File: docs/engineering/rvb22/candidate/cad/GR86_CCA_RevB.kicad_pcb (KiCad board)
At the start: 4 copper layers, 88.3 x 61.3 mm, 199 parts, among them J201 TC2030-IDC-NL / UART, J202 RESET — short to reset, J203 BOOT — hold low on reset, J401 U.FL-R-SMT-1(80), Q101 STD25NF20 /200V, U101 LTC4367HMS8#WTRPBF, U121 LM5164DDAR, U151 LM63615DQPWPRQ1, U201 ESP32-S3-WROOM-1-N8R2, U202 TPS3808G33-Q1 3.07V RESET, U301 TCAN3403DRBRQ1, U401 PA1616D, U402 SN74LVC2G125DCUR, U403 MIC5504-3.3YM5-TR, U404 SN74LVC2G125DCUR, U501 TPS26600PWPR, U502 OPA2333AIDR

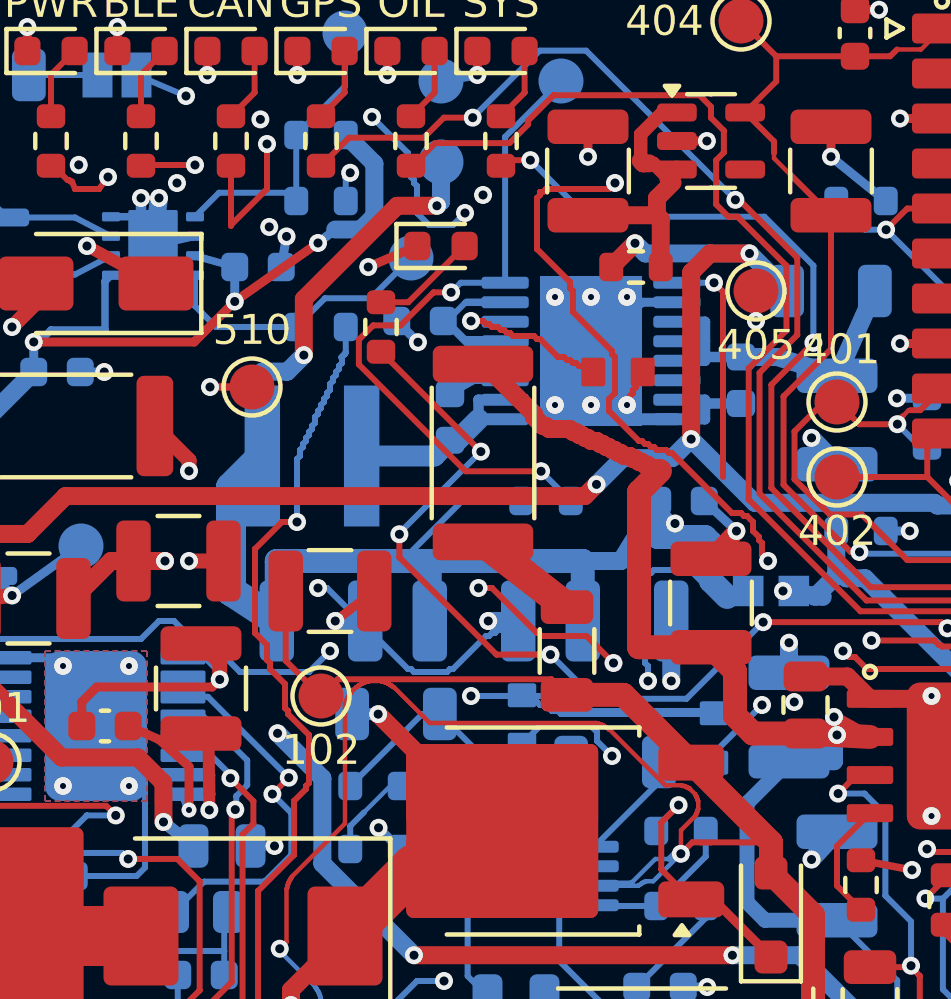
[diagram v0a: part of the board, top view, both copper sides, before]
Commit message: fix(cca): apply I08 native routing and source integrity corrections
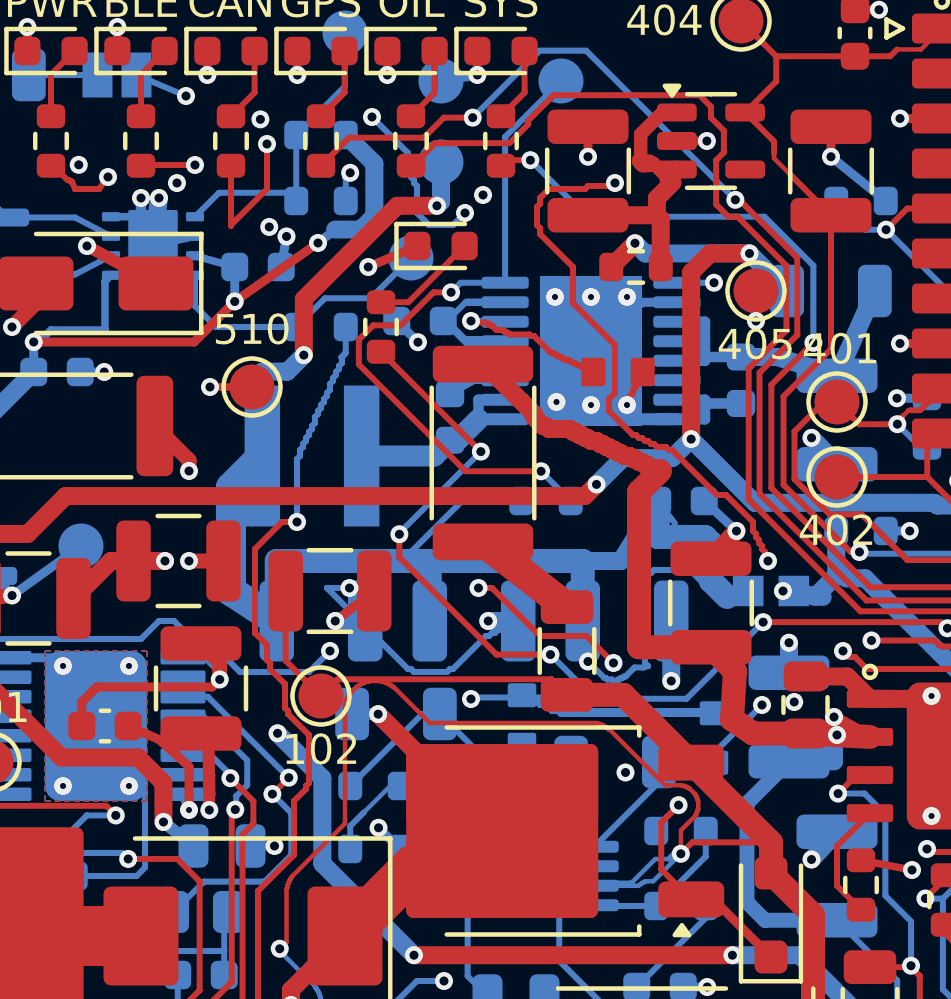
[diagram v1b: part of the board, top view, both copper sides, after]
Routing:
- net GND: track 197.0 -> 179.3 mm
- net 3V3_FB_ADJ: track 70.7 -> 64.0 mm
- net +3V3: track 331.9 -> 338.3 mm
- net 3V3_SOURCE: track 68.7 -> 72.9 mm, vias 5 -> 4
- net 3V3_VCC_INTERNAL: track 11.6 -> 10.3 mm

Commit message: fix(cca): route rail around mechanical holes and resolve native model exports
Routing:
- net +3V3: track 338.3 -> 350.1 mm
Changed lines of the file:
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@@
 (segment (start 40.7 19.6) (end 40.8 19.7) (width 0.2) (layer "F.Cu") (net 132))
 (segment (start 40.8 19.7) (end 40.9 20.0) (width 0.2) (layer "F.Cu") (net 132))
-(segment (start 57.9 16.8) (end 58.0 16.5) (width 2.0) (layer "In2.Cu") (net 1))
-(segment (start 58.0 16.5) (end 63.7 10.8) (width 2.0) (layer "In2.Cu") (net 1))
-(segment (start 63.7 10.8) (end 63.7 7.7) (width 2.0) (layer "In2.Cu") (net 1))
-(segment (start 63.7 7.7) (end 63.8 7.6) (width 2.0) (layer "In2.Cu") (net 1))
-(segment (start 63.8 7.6) (end 63.8 7.4) (width 2.0) (layer "In2.Cu") (net 1))
-(segment (start 63.8 7.4) (end 64.3 6.9) (width 2.0) (layer "In2.Cu") (net 1))
-(segment (start 64.3 6.9) (end 64.3 6.1) (width 2.0) (layer "In2.Cu") (net 1))
-(segment (start 64.3 6.1) (end 64.4 6.0) (width 2.0) (layer "In2.Cu") (net 1))
-(segment (start 64.4 6.0) (end 64.4 5.9) (width 2.0) (layer "In2.Cu") (net 1))
-(segment (start 64.4 5.9) (end 64.5 5.8) (width 2.0) (layer "In2.Cu") (net 1))
-(segment (start 64.5 5.8) (end 64.5 5.7) (width 2.0) (layer "In2.Cu") (net 1))
-(segment (start 64.5 5.7) (end 65.0 5.2) (width 2.0) (layer "In2.Cu") (net 1))
-(segment (start 65.0 5.2) (end 65.1 5.2) (width 2.0) (layer "In2.Cu") (net 1))
-(segment (start 65.1 5.2) (end 65.2 5.1) (width 2.0) (layer "In2.Cu") (net 1))
-(segment (start 65.2 5.1) (end 65.5 5.1) (width 2.0) (layer "In2.Cu") (net 1))
-(segment (start 65.5 5.1) (end 65.6 5.0) (width 2.0) (layer "In2.Cu") (net 1))
-(segment (start 65.6 5.0) (end 66.4 5.0) (width 2.0) (layer "In2.Cu") (net 1))
-(segment (start 66.4 5.0) (end 70.6 9.2) (width 2.0) (layer "In2.Cu") (net 1))
-(segment (start 70.6 9.2) (end 70.7 9.2) (width 2.0) (layer "In2.Cu") (net 1))
-(segment (start 70.7 9.2) (end 70.8 9.3) (width 2.0) (layer "In2.Cu") (net 1))
-(segment (start 70.8 9.3) (end 70.9 9.3) (width 2.0) (layer "In2.Cu") (net 1))
-(segment (start 70.9 9.3) (end 71.0 9.4) (width 2.0) (layer "In2.Cu") (net 1))
-(segment (start 71.0 9.4) (end 71.1 9.4) (width 2.0) (layer "In2.Cu") (net 1))
-(segment (start 71.1 9.4) (end 71.2 9.5) (width 2.0) (layer "In2.Cu") (net 1))
-(segment (start 71.2 9.5) (end 71.5 9.6) (width 2.0) (layer "In2.Cu") (net 1))
 (segment (start 34.9 23.35) (end 35.6 24.05) (width 0.2) (layer "In2.Cu") (net 5))
 (segment (start 35.6 24.05) (end 36.55 24.05) (width 0.2) (layer "In2.Cu") (net 5))
@@
 (segment (start 34.9 13.6) (end 34.95 13.65) (width 0.2) (layer "F.Cu") (net 131))
 (segment (start 34.95 13.65) (end 35.075 13.7) (width 0.2) (layer "F.Cu") (net 131))
+(segment (start 57.9 16.8) (end 58.0 16.5) (width 2.0) (layer "In2.Cu") (net 1))
+(segment (start 58.0 16.5) (end 63.7 10.8) (width 2.0) (layer "In2.Cu") (net 1))
+(segment (start 63.7 10.8) (end 63.7 7.7) (width 2.0) (layer "In2.Cu") (net 1))
+(segment (start 63.7 7.7) (end 63.8 7.6) (width 2.0) (layer "In2.Cu") (net 1))
+(segment (start 63.8 7.6) (end 63.8 7.4) (width 2.0) (layer "In2.Cu") (net 1))
+(segment (start 63.8 7.4) (end 64.3 6.9) (width 2.0) (layer "In2.Cu") (net 1))
+(segment (start 64.3 6.9) (end 64.3 6.1) (width 2.0) (layer "In2.Cu") (net 1))
+(segment (start 64.3 6.1) (end 64.4 6.0) (width 2.0) (layer "In2.Cu") (net 1))
+(segment (start 64.4 6.0) (end 64.4 5.9) (width 2.0) (layer "In2.Cu") (net 1))
+(segment (start 64.4 5.9) (end 64.5 5.8) (width 2.0) (layer "In2.Cu") (net 1))
+(segment (start 64.5 5.8) (end 64.5 5.7) (width 2.0) (layer "In2.Cu") (net 1))
+(segment (start 64.5 5.7) (end 65.0 5.2) (width 2.0) (layer "In2.Cu") (net 1))
+(segment (start 65.0 5.2) (end 65.1 5.2) (width 2.0) (layer "In2.Cu") (net 1))
+(segment (start 65.1 5.2) (end 65.2 5.1) (width 2.0) (layer "In2.Cu") (net 1))
+(segment (start 65.2 5.1) (end 65.5 5.1) (width 2.0) (layer "In2.Cu") (net 1))
+(segment (start 65.5 5.1) (end 65.6 5.0) (width 2.0) (layer "In2.Cu") (net 1))
+(segment (start 65.6 5.0) (end 66.7 5.0) (width 2.0) (layer "In2.Cu") (net 1))
+(segment (start 66.7 5.0) (end 68.1 3.6) (width 2.0) (layer "In2.Cu") (net 1))
+(segment (start 68.1 3.6) (end 68.2 3.6) (width 2.0) (layer "In2.Cu") (net 1))
+(segment (start 68.2 3.6) (end 68.4 3.4) (width 2.0) (layer "In2.Cu") (net 1))
+(segment (start 68.4 3.4) (end 68.5 3.4) (width 2.0) (layer "In2.Cu") (net 1))
+(segment (start 68.5 3.4) (end 68.6 3.3) (width 2.0) (layer "In2.Cu") (net 1))
+(segment (start 68.6 3.3) (end 68.9 3.3) (width 2.0) (layer "In2.Cu") (net 1))
+(segment (start 68.9 3.3) (end 69.0 3.2) (width 2.0) (layer "In2.Cu") (net 1))
+(segment (start 69.0 3.2) (end 73.9 3.2) (width 2.0) (layer "In2.Cu") (net 1))
+(segment (start 73.9 3.2) (end 74.0 3.3) (width 2.0) (layer "In2.Cu") (net 1))
+(segment (start 74.0 3.3) (end 74.2 3.3) (width 2.0) (layer "In2.Cu") (net 1))
+(segment (start 74.2 3.3) (end 74.3 3.4) (width 2.0) (layer "In2.Cu") (net 1))
+(segment (start 74.3 3.4) (end 74.4 3.4) (width 2.0) (layer "In2.Cu") (net 1))
+(segment (start 74.4 3.4) (end 74.5 3.5) (width 2.0) (layer "In2.Cu") (net 1))
+(segment (start 74.5 3.5) (end 74.6 3.5) (width 2.0) (layer "In2.Cu") (net 1))
+(segment (start 74.6 3.5) (end 75.0 3.9) (width 2.0) (layer "In2.Cu") (net 1))
+(segment (start 75.0 3.9) (end 75.0 4.0) (width 2.0) (layer "In2.Cu") (net 1))
+(segment (start 75.0 4.0) (end 75.1 4.1) (width 2.0) (layer "In2.Cu") (net 1))
+(segment (start 75.1 4.1) (end 75.1 4.2) (width 2.0) (layer "In2.Cu") (net 1))
+(segment (start 75.1 4.2) (end 75.2 4.3) (width 2.0) (layer "In2.Cu") (net 1))
+(segment (start 75.2 4.3) (end 75.2 4.4) (width 2.0) (layer "In2.Cu") (net 1))
+(segment (start 75.2 4.4) (end 75.3 4.5) (width 2.0) (layer "In2.Cu") (net 1))
+(segment (start 75.3 4.5) (end 75.3 4.6) (width 2.0) (layer "In2.Cu") (net 1))
+(segment (start 75.3 4.6) (end 75.8 5.1) (width 2.0) (layer "In2.Cu") (net 1))
+(segment (start 75.8 5.1) (end 75.8 5.2) (width 2.0) (layer "In2.Cu") (net 1))
+(segment (start 75.8 5.2) (end 76.0 5.4) (width 2.0) (layer "In2.Cu") (net 1))
+(segment (start 76.0 5.4) (end 76.0 5.6) (width 2.0) (layer "In2.Cu") (net 1))
+(segment (start 76.0 5.6) (end 76.1 5.7) (width 2.0) (layer "In2.Cu") (net 1))
+(segment (start 76.1 5.7) (end 76.1 6.3) (width 2.0) (layer "In2.Cu") (net 1))
+(segment (start 76.1 6.3) (end 76.0 6.4) (width 2.0) (layer "In2.Cu") (net 1))
+(segment (start 76.0 6.4) (end 76.0 6.6) (width 2.0) (layer "In2.Cu") (net 1))
+(segment (start 76.0 6.6) (end 75.8 6.8) (width 2.0) (layer "In2.Cu") (net 1))
+(segment (start 75.8 6.8) (end 75.8 6.9) (width 2.0) (layer "In2.Cu") (net 1))
+(segment (start 75.8 6.9) (end 75.3 7.4) (width 2.0) (layer "In2.Cu") (net 1))
+(segment (start 75.3 7.4) (end 75.3 7.5) (width 2.0) (layer "In2.Cu") (net 1))
+(segment (start 75.3 7.5) (end 75.2 7.6) (width 2.0) (layer "In2.Cu") (net 1))
+(segment (start 75.2 7.6) (end 75.2 7.7) (width 2.0) (layer "In2.Cu") (net 1))
+(segment (start 75.2 7.7) (end 75.1 7.8) (width 2.0) (layer "In2.Cu") (net 1))
+(segment (start 75.1 7.8) (end 75.1 7.9) (width 2.0) (layer "In2.Cu") (net 1))
+(segment (start 75.1 7.9) (end 75.0 8.0) (width 2.0) (layer "In2.Cu") (net 1))
+(segment (start 75.0 8.0) (end 75.0 8.1) (width 2.0) (layer "In2.Cu") (net 1))
+(segment (start 75.0 8.1) (end 74.6 8.5) (width 2.0) (layer "In2.Cu") (net 1))
+(segment (start 74.6 8.5) (end 74.5 8.5) (width 2.0) (layer "In2.Cu") (net 1))
+(segment (start 74.5 8.5) (end 74.4 8.6) (width 2.0) (layer "In2.Cu") (net 1))
+(segment (start 74.4 8.6) (end 74.3 8.6) (width 2.0) (layer "In2.Cu") (net 1))
+(segment (start 74.3 8.6) (end 74.2 8.7) (width 2.0) (layer "In2.Cu") (net 1))
+(segment (start 74.2 8.7) (end 74.0 8.7) (width 2.0) (layer "In2.Cu") (net 1))
+(segment (start 74.0 8.7) (end 73.9 8.8) (width 2.0) (layer "In2.Cu") (net 1))
+(segment (start 73.9 8.8) (end 73.2 8.8) (width 2.0) (layer "In2.Cu") (net 1))
+(segment (start 73.2 8.8) (end 73.1 8.9) (width 2.0) (layer "In2.Cu") (net 1))
+(segment (start 73.1 8.9) (end 73.0 8.9) (width 2.0) (layer "In2.Cu") (net 1))
+(segment (start 73.0 8.9) (end 72.9 9.0) (width 2.0) (layer "In2.Cu") (net 1))
+(segment (start 72.9 9.0) (end 72.8 9.0) (width 2.0) (layer "In2.Cu") (net 1))
+(segment (start 72.8 9.0) (end 72.7 9.1) (width 2.0) (layer "In2.Cu") (net 1))
+(segment (start 72.7 9.1) (end 72.3 9.1) (width 2.0) (layer "In2.Cu") (net 1))
+(segment (start 72.3 9.1) (end 72.2 9.2) (width 2.0) (layer "In2.Cu") (net 1))
+(segment (start 72.2 9.2) (end 72.0 9.2) (width 2.0) (layer "In2.Cu") (net 1))
+(segment (start 72.0 9.2) (end 71.9 9.3) (width 2.0) (layer "In2.Cu") (net 1))
+(segment (start 71.9 9.3) (end 71.8 9.3) (width 2.0) (layer "In2.Cu") (net 1))
+(segment (start 71.8 9.3) (end 71.5 9.6) (width 2.0) (layer "In2.Cu") (net 1))
 )

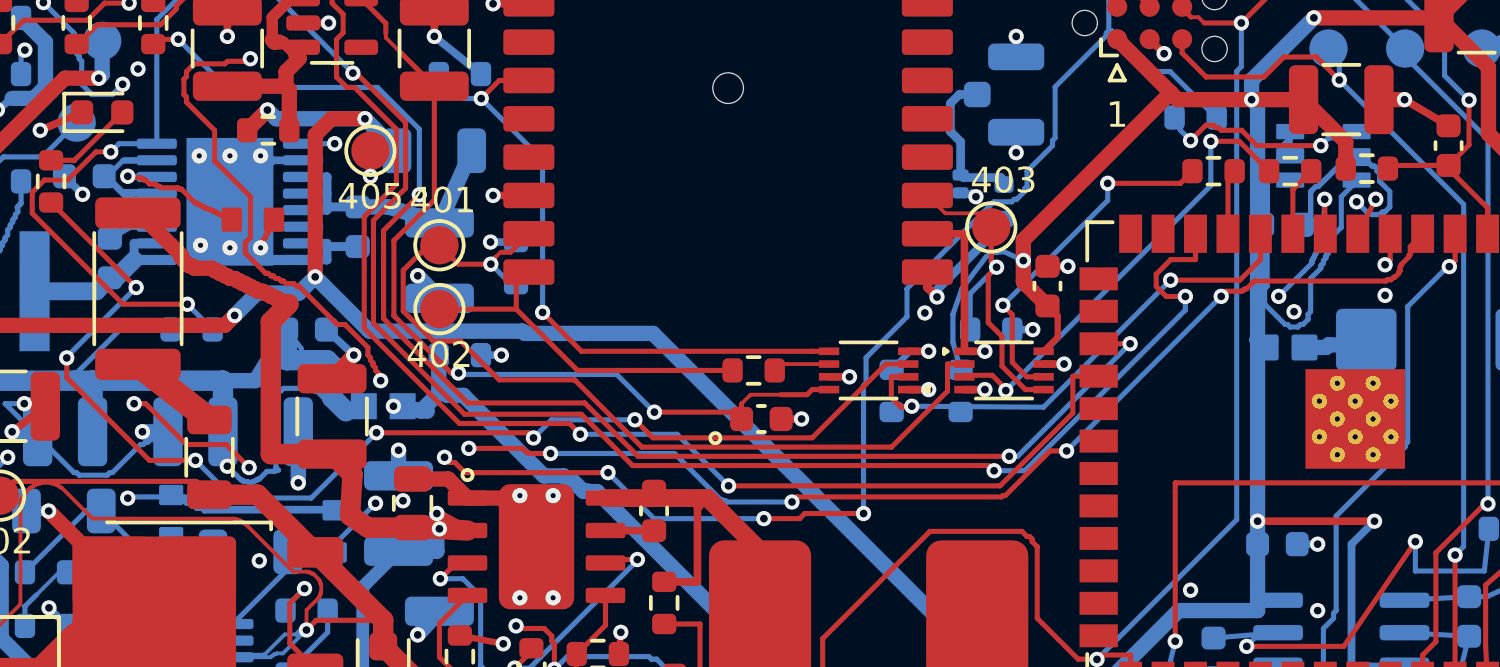
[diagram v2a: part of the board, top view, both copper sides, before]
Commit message: fix(cca): remove duplicate rail branch and select explicit native footprint exporter
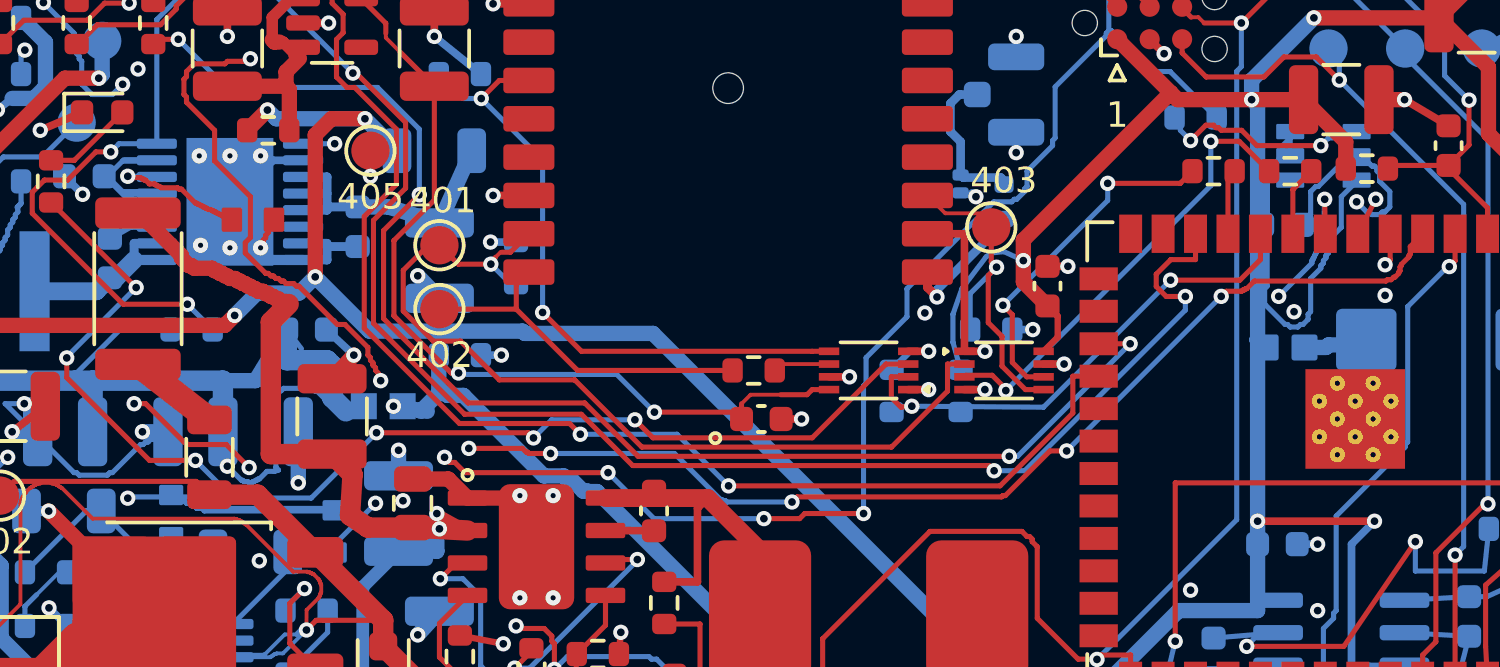
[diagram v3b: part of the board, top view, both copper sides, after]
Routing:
- net +3V3: track 350.1 -> 347.2 mm
- net GND: track 179.3 -> 176.6 mm
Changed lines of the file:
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@@
 (segment (start 77.0 13.8) (end 77.0 13.9) (width 0.2) (layer "B.Cu") (net 30))
 (segment (start 77.0 13.9) (end 76.97500000000001 13.9) (width 0.2) (layer "B.Cu") (net 30))
-(segment (start 76.97500000000001 13.9) (end 77.0 13.9) (width 0.2) (layer "B.Cu") (net 30))
 (segment (start 77.0 13.9) (end 77.1 13.8) (width 0.2) (layer "B.Cu") (net 30))
 (segment (start 77.1 13.8) (end 77.1 13.7) (width 0.2) (layer "B.Cu") (net 30))
 (segment (start 77.1 13.7) (end 77.3 13.5) (width 0.2) (layer "B.Cu") (net 30))
-(segment (start 77.3 13.5) (end 77.3 12.6) (width 0.2) (layer "B.Cu") (net 30))
-(segment (start 77.3 12.6) (end 77.5 12.4) (width 0.2) (layer "B.Cu") (net 30))
-(segment (start 77.5 12.4) (end 77.6 12.4) (width 0.2) (layer "B.Cu") (net 30))
-(segment (start 77.6 12.4) (end 78.4 11.6) (width 0.2) (layer "B.Cu") (net 30))
-(segment (start 78.4 11.6) (end 78.5 11.6) (width 0.2) (layer "B.Cu") (net 30))
-(segment (start 78.5 11.6) (end 78.6 11.5) (width 0.2) (layer "B.Cu") (net 30))
 (segment (start 78.6 11.5) (end 79.6 11.5) (width 0.2) (layer "B.Cu") (net 30))
 (segment (start 79.6 11.5) (end 79.7 11.6) (width 0.2) (layer "B.Cu") (net 30))
@@
 (segment (start 76.5 10.25) (end 76.5 11.2) (width 0.2) (layer "B.Cu") (net 1))
 (segment (start 76.5 11.2) (end 76.2 11.2) (width 0.2) (layer "B.Cu") (net 1))
-(segment (start 76.2 11.2) (end 75.7 11.7) (width 0.2) (layer "B.Cu") (net 1))
-(segment (start 75.7 11.7) (end 75.7 11.8) (width 0.2) (layer "B.Cu") (net 1))
-(segment (start 75.7 11.8) (end 75.6 11.9) (width 0.2) (layer "B.Cu") (net 1))
 (segment (start 75.6 11.9) (end 75.6 16.3) (width 0.2) (layer "B.Cu") (net 1))
 (segment (start 75.6 16.3) (end 75.5 16.4) (width 0.2) (layer "B.Cu") (net 1))
@@
 (segment (start 79.0 12.2) (end 79.1 12.1) (width 0.2) (layer "B.Cu") (net 1))
 (segment (start 79.1 12.1) (end 79.1 12.149999999999999) (width 0.2) (layer "B.Cu") (net 1))
-(segment (start 75.425 13.9) (end 75.4 13.9) (width 0.2) (layer "B.Cu") (net 1))
 (segment (start 75.4 13.9) (end 75.4 9.8) (width 0.2) (layer "B.Cu") (net 1))
 (segment (start 75.4 9.8) (end 75.3 9.7) (width 0.2) (layer "B.Cu") (net 1))
@@
 (segment (start 86.5 14.8) (end 86.6 14.7) (width 0.6) (layer "F.Cu") (net 30))
 (segment (start 85.8 16.3) (end 85.9 16.2) (width 0.6) (layer "F.Cu") (net 30))
-(segment (start 71.5 9.6) (end 71.8 9.3) (width 2.0) (layer "In2.Cu") (net 1))
 (segment (start 34.5 24.5) (end 35.0 25.0) (width 0.2) (layer "B.Cu") (net 132))
 (segment (start 36.6 14.0) (end 36.5 14.1) (width 0.2) (layer "F.Cu") (net 30))
@@
 (segment (start 30.4 11.8) (end 30.8 11.4) (width 0.2) (layer "B.Cu") (net 7))
 (segment (start 63.55 8.8) (end 64.25 8.8) (width 0.34) (layer "B.Cu") (net 34))
-(segment (start 71.9 9.3) (end 72.0 9.2) (width 2.0) (layer "In2.Cu") (net 1))
 (segment (start 37.5 24.6) (end 37.4 24.5) (width 0.2) (layer "In2.Cu") (net 5))
 (segment (start 40.5 24.6) (end 37.5 24.6) (width 0.2) (layer "In2.Cu") (net 5))
@@
 (segment (start 50.3 20.1) (end 50.6 20.1) (width 2.0) (layer "In2.Cu") (net 1))
 (segment (start 31.4 13.4375) (end 31.4 13.4) (width 0.6) (layer "F.Cu") (net 17))
-(segment (start 72.2 9.2) (end 72.3 9.1) (width 2.0) (layer "In2.Cu") (net 1))
 (segment (start 38.2 20.3) (end 38.3 20.4) (width 0.2) (layer "B.Cu") (net 5))
 (segment (start 31.7 13.1) (end 31.8 13.2) (width 0.2) (layer "B.Cu") (net 7))
-(segment (start 39.1 25.075) (end 39.1 25.1) (width 0.2) (layer "B.Cu") (net 132))
 (segment (start 39.1 25.1) (end 34.0 25.1) (width 0.2) (layer "B.Cu") (net 132))
 (segment (start 53.2 18.9) (end 53.3 18.9) (width 2.0) (layer "In2.Cu") (net 1))
-(segment (start 71.8 9.3) (end 71.9 9.3) (width 2.0) (layer "In2.Cu") (net 1))
 (segment (start 37.2 16.9) (end 37.3 17.0) (width 0.6) (layer "F.Cu") (net 17))
 (segment (start 86.0 15.9) (end 86.1 15.8) (width 0.6) (layer "F.Cu") (net 30))
@@
 (segment (start 51.4 19.7) (end 51.5 19.7) (width 2.0) (layer "In2.Cu") (net 1))
 (segment (start 36.4 14.3) (end 36.4 14.4) (width 0.2) (layer "F.Cu") (net 30))
-(segment (start 32.1375 13.325) (end 32.1 13.3) (width 0.2) (layer "B.Cu") (net 7))
 (segment (start 32.2 22.2) (end 32.3 22.1) (width 0.2) (layer "B.Cu") (net 30))
 (segment (start 30.2 23.7) (end 30.3 23.6) (width 0.2) (layer "B.Cu") (net 30))
@@
 (segment (start 26.0 21.7) (end 25.9 21.8) (width 0.2) (layer "In2.Cu") (net 132))
 (segment (start 33.5 22.0) (end 33.4 22.1) (width 0.2) (layer "In2.Cu") (net 132))
-(segment (start 72.0 9.2) (end 72.2 9.2) (width 2.0) (layer "In2.Cu") (net 1))
 (segment (start 51.9 19.5) (end 52.0 19.5) (width 2.0) (layer "In2.Cu") (net 1))
 (segment (start 48.4 20.6) (end 49.6 20.6) (width 2.0) (layer "In2.Cu") (net 1))
@@
 (segment (start 72.8 9.0) (end 72.7 9.1) (width 2.0) (layer "In2.Cu") (net 1))
 (segment (start 72.7 9.1) (end 72.3 9.1) (width 2.0) (layer "In2.Cu") (net 1))
-(segment (start 72.3 9.1) (end 72.2 9.2) (width 2.0) (layer "In2.Cu") (net 1))
-(segment (start 72.2 9.2) (end 72.0 9.2) (width 2.0) (layer "In2.Cu") (net 1))
-(segment (start 72.0 9.2) (end 71.9 9.3) (width 2.0) (layer "In2.Cu") (net 1))
-(segment (start 71.9 9.3) (end 71.8 9.3) (width 2.0) (layer "In2.Cu") (net 1))
-(segment (start 71.8 9.3) (end 71.5 9.6) (width 2.0) (layer "In2.Cu") (net 1))
 )
